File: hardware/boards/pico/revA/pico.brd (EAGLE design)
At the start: 45 x 104 mm, 151 parts, among them IC2 TPS6300, J12 3.5mm TRRS Jack, J3 MOLEX_105450-0101MOLEX_105450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, Q2 ON_SEMI_MMBT5551LT1GON_SEMI_M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, U1 VS1053-L, U2 MICROCHIP_MCP73831T-2ATI-OTMI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

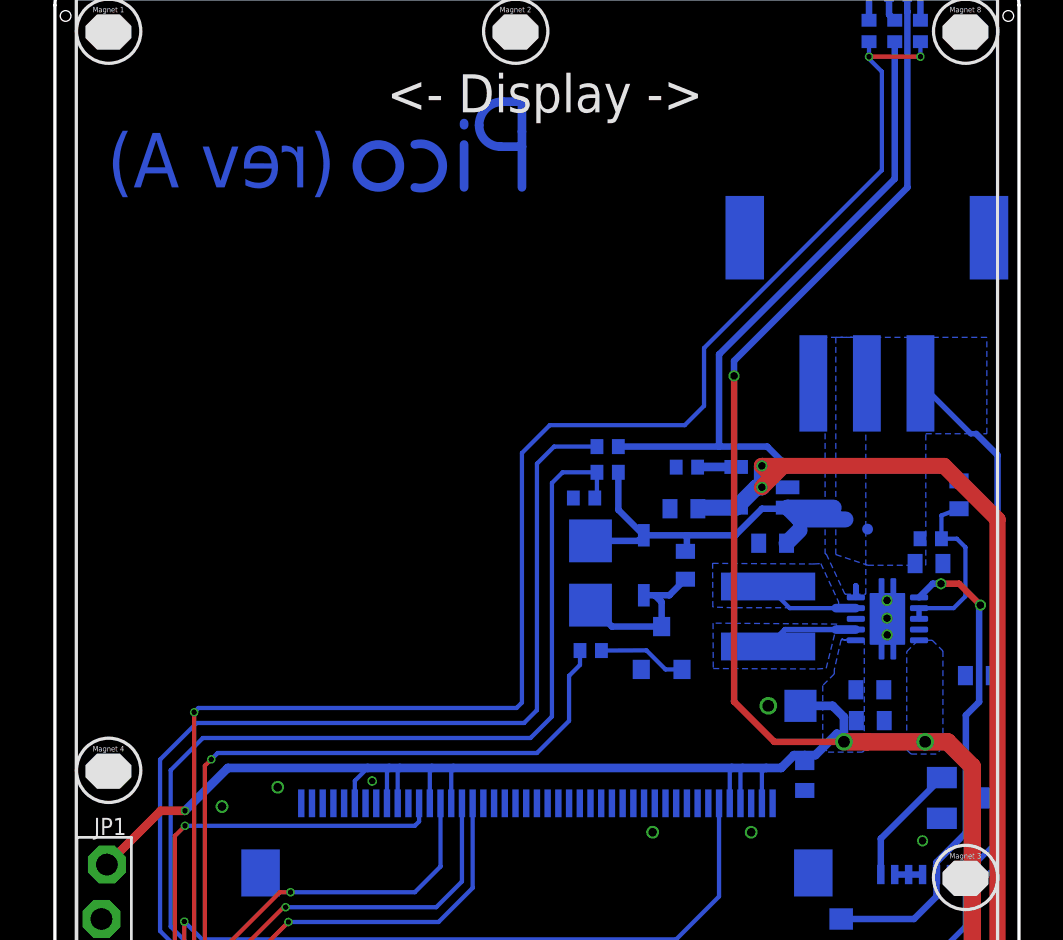
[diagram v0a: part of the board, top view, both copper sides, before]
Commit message: pico: add some (bad) art
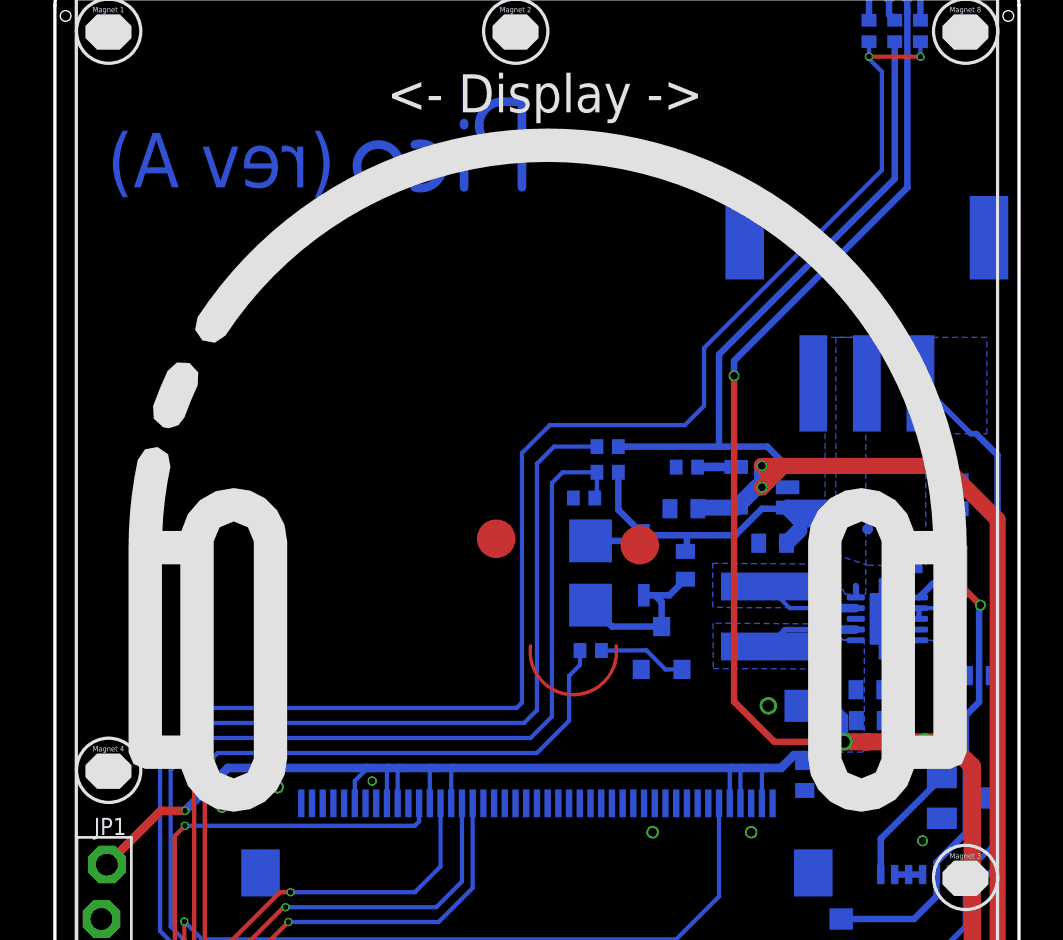
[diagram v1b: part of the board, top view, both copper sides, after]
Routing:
- net N$7: track 0.00 -> 4.00 mm

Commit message: pico: K -> k
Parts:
- R16: value 100KΩ -> 100kΩ
- R8: value 1.5KΩ -> 1.5kΩ
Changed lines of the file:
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@@
 <drawing>
 <settings>
-<setting alwaysvectorfont="yes"/>
+<setting alwaysvectorfont="no"/>
 <setting verticaltext="up"/>
 </settings>
@@
 <attribute name="VOLTAGE_-_DC_REVERSE_(VR)_(MAX)" value="75V" x="-3.01" y="3.36" size="1.778" layer="28" rot="MR270" display="off"/>
 </element>
-<element name="R8" library="rcl" library_urn="urn:adsk.eagle:library:334" package="R0402" package3d_urn="urn:adsk.eagle:package:23547/3" value="1.5KΩ" x="2.51" y="-0.62" smashed="yes" rot="MR180">
+<element name="R8" library="rcl" library_urn="urn:adsk.eagle:library:334" package="R0402" package3d_urn="urn:adsk.eagle:package:23547/3" value="1.5kΩ" x="2.51" y="-0.62" smashed="yes" rot="MR180">
 <attribute name="NAME" x="1.451" y="-0.371" size="0.4" layer="26" rot="SMR270"/>
 <attribute name="SPICEPREFIX" value="R" x="2.51" y="-0.62" size="1.778" layer="28" rot="MR180" display="off"/>
@@
 <attribute name="VALUE" x="-17.025" y="-29.66" size="1.27" layer="27" rot="R90"/>
 </element>
-<element name="R16" library="rcl" library_urn="urn:adsk.eagle:library:334" package="R0402" package3d_urn="urn:adsk.eagle:package:23547/3" value="100KΩ" x="10" y="-39" smashed="yes" rot="MR180">
+<element name="R16" library="rcl" library_urn="urn:adsk.eagle:library:334" package="R0402" package3d_urn="urn:adsk.eagle:package:23547/3" value="100kΩ" x="10" y="-39" smashed="yes" rot="MR180">
 <attribute name="NAME" x="9.795" y="-38.235" size="0.4" layer="26" rot="MR180"/>
 <attribute name="SPICEPREFIX" value="R" x="10" y="-39" size="1.778" layer="28" rot="MR180" display="off"/>
